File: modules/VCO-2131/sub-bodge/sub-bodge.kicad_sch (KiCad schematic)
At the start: 2 parts, among them U1 CD4013, U2 SN74HCS74

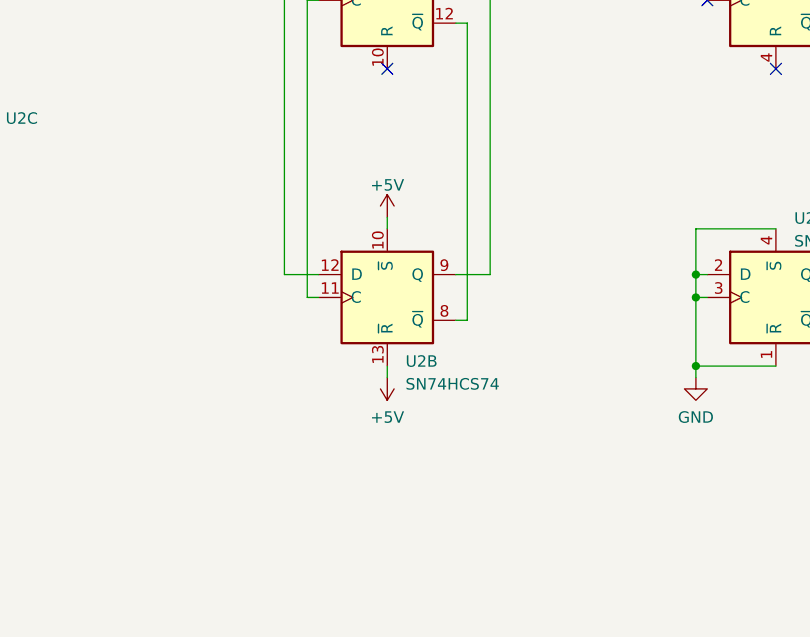
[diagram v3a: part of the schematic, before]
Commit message: VCO sub fix - try again
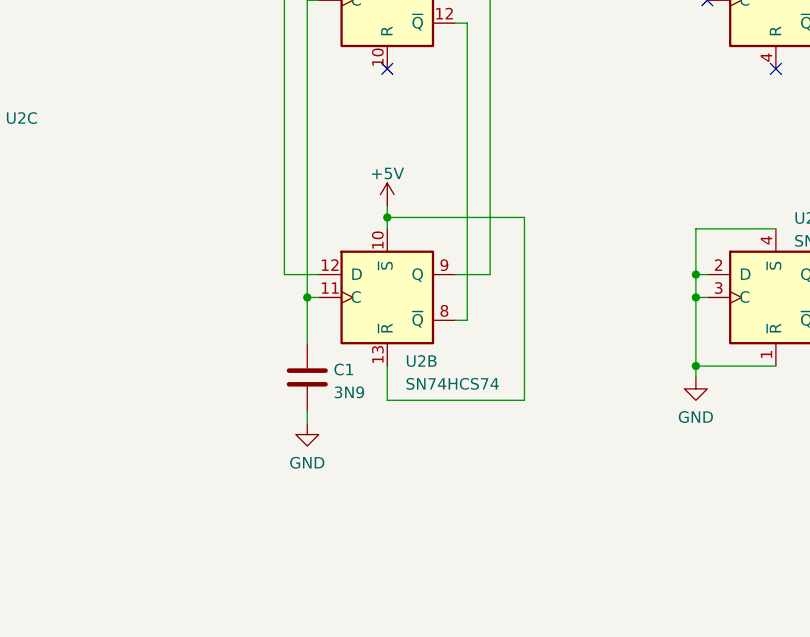
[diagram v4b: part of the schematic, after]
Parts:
- added C1: 3N9, -lmp-misc:C_Rect_Kemet_L7.2mm_W2.5mm_P5mm, symbol -lmp:CF
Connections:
- net GND: now also C1.2
- net at U1.11 (C), U2.11 (C): now also C1.1
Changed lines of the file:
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@@
   (junction (at 177.8 104.14) (diameter 0) (color 0 0 0 0)
+  )
+  (junction (at 143.51 97.79) (diameter 0) (color 0 0 0 0)
+  )
+  (junction (at 134.62 106.68) (diameter 0) (color 0 0 0 0)
   )
   (junction (at 177.8 106.68) (diameter 0) (color 0 0 0 0)
@@
     (stroke (width 0) (type default) (color 0 0 0 0))
   )
+  (wire (pts (xy 143.51 96.52) (xy 143.51 97.79))
+    (stroke (width 0) (type default) (color 0 0 0 0))
+  )
+  (wire (pts (xy 143.51 97.79) (xy 158.75 97.79))
+    (stroke (width 0) (type default) (color 0 0 0 0))
+  )
+  (wire (pts (xy 158.75 97.79) (xy 158.75 118.11))
+    (stroke (width 0) (type default) (color 0 0 0 0))
+  )
+  (wire (pts (xy 134.62 119.38) (xy 134.62 120.65))
+    (stroke (width 0) (type default) (color 0 0 0 0))
+  )
+  (wire (pts (xy 132.08 104.14) (xy 135.89 104.14))
+    (stroke (width 0) (type default) (color 0 0 0 0))
+  )
+  (wire (pts (xy 143.51 114.3) (xy 143.51 118.11))
+    (stroke (width 0) (type default) (color 0 0 0 0))
+  )
+  (wire (pts (xy 78.74 77.47) (xy 78.74 80.01))
+    (stroke (width 0) (type default) (color 0 0 0 0))
+  )
   (wire (pts (xy 143.51 97.79) (xy 143.51 99.06))
     (stroke (width 0) (type default) (color 0 0 0 0))
   )
-  (wire (pts (xy 132.08 104.14) (xy 135.89 104.14))
-    (stroke (width 0) (type default) (color 0 0 0 0))
-  )
-  (wire (pts (xy 143.51 114.3) (xy 143.51 115.57))
-    (stroke (width 0) (type default) (color 0 0 0 0))
-  )
-  (wire (pts (xy 78.74 77.47) (xy 78.74 80.01))
-    (stroke (width 0) (type default) (color 0 0 0 0))
-  )
   (wire (pts (xy 177.8 114.3) (xy 186.69 114.3))
     (stroke (width 0) (type default) (color 0 0 0 0))
@@
     (stroke (width 0) (type default) (color 0 0 0 0))
   )
+  (wire (pts (xy 143.51 118.11) (xy 158.75 118.11))
+    (stroke (width 0) (type default) (color 0 0 0 0))
+  )
   (wire (pts (xy 152.4 76.2) (xy 152.4 109.22))
     (stroke (width 0) (type default) (color 0 0 0 0))
   )
   (wire (pts (xy 177.8 104.14) (xy 179.07 104.14))
+    (stroke (width 0) (type default) (color 0 0 0 0))
+  )
+  (wire (pts (xy 134.62 106.68) (xy 134.62 111.76))
     (stroke (width 0) (type default) (color 0 0 0 0))
   )
@@
   (symbol (lib_id "-lmp-power:+5V") (at 78.74 77.47 0) (unit 1)
     (in_bom yes) (on_board yes) (fields_autoplaced)
-    (property "Reference" "#PWR0108" (id 0) (at 78.74 81.28 0)
+    (property "Reference" "#PWR01" (id 0) (at 78.74 81.28 0)
       (effects (font (size 1.27 1.27)) hide)
     )
@@
     (pin "1")
   )
+  (symbol (lib_id "-lmp:CF") (at 134.62 115.57 0) (unit 1)
+    (in_bom yes) (on_board yes) (fields_autoplaced)
+    (property "Reference" "C1" (id 0) (at 137.541 114.7353 0)
+      (effects (font (size 1.27 1.27)) (justify left))
+    )
+    (property "Value" "3N9" (id 1) (at 137.541 117.2722 0)
+      (effects (font (size 1.27 1.27)) (justify left))
+    )
+    (property "Footprint" "-lmp-misc:C_Rect_Kemet_L7.2mm_W2.5mm_P5mm" (id 2) (at 135.5852 119.38 0)
+      (effects (font (size 1.27 1.27)) hide)
+    )
+    (property "Datasheet" "~" (id 3) (at 134.62 115.57 0)
+      (effects (font (size 1.27 1.27)) hide)
+    )
+    (pin "1")
+    (pin "2")
+  )
   (symbol (lib_id "-lmp-IC-misc:CD4013") (at 186.69 73.66 0) (unit 1)
     (in_bom yes) (on_board yes) (fields_autoplaced)
@@
   (symbol (lib_id "-lmp-power:GND") (at 78.74 97.79 0) (unit 1)
     (in_bom yes) (on_board yes) (fields_autoplaced)
-    (property "Reference" "#PWR0107" (id 0) (at 78.74 104.14 0)
+    (property "Reference" "#PWR02" (id 0) (at 78.74 104.14 0)
       (effects (font (size 1.27 1.27)) hide)
     )
@@
     (pin "7")
   )
-  (symbol (lib_id "-lmp-power:+5V") (at 143.51 97.79 0) (unit 1)
-    (in_bom yes) (on_board yes) (fields_autoplaced)
-    (property "Reference" "#PWR0106" (id 0) (at 143.51 101.6 0)
-      (effects (font (size 1.27 1.27)) hide)
-    )
-    (property "Value" "+5V" (id 1) (at 143.51 94.2142 0))
-    (property "Footprint" "" (id 2) (at 143.51 97.79 0)
-      (effects (font (size 1.27 1.27)) hide)
-    )
-    (property "Datasheet" "" (id 3) (at 143.51 97.79 0)
+  (symbol (lib_id "-lmp-power:+5V") (at 143.51 96.52 0) (unit 1)
+    (in_bom yes) (on_board yes) (fields_autoplaced)
+    (property "Reference" "#PWR04" (id 0) (at 143.51 100.33 0)
+      (effects (font (size 1.27 1.27)) hide)
+    )
+    (property "Value" "+5V" (id 1) (at 143.51 92.9442 0))
+    (property "Footprint" "" (id 2) (at 143.51 96.52 0)
+      (effects (font (size 1.27 1.27)) hide)
+    )
+    (property "Datasheet" "" (id 3) (at 143.51 96.52 0)
       (effects (font (size 1.27 1.27)) hide)
     )
@@
   (symbol (lib_id "-lmp-power:GND") (at 177.8 115.57 0) (unit 1)
     (in_bom yes) (on_board yes) (fields_autoplaced)
-    (property "Reference" "#PWR0102" (id 0) (at 177.8 121.92 0)
+    (property "Reference" "#PWR05" (id 0) (at 177.8 121.92 0)
       (effects (font (size 1.27 1.27)) hide)
     )
@@
     (pin "1")
   )
-  (symbol (lib_id "-lmp-power:+5V") (at 143.51 115.57 180) (unit 1)
-    (in_bom yes) (on_board yes) (fields_autoplaced)
-    (property "Reference" "#PWR0105" (id 0) (at 143.51 111.76 0)
-      (effects (font (size 1.27 1.27)) hide)
-    )
-    (property "Value" "+5V" (id 1) (at 143.51 120.0134 0))
-    (property "Footprint" "" (id 2) (at 143.51 115.57 0)
-      (effects (font (size 1.27 1.27)) hide)
-    )
-    (property "Datasheet" "" (id 3) (at 143.51 115.57 0)
-      (effects (font (size 1.27 1.27)) hide)
-    )
-    (pin "1")
-  )
   (symbol (lib_id "-lmp-IC-misc:SN74HCS74") (at 186.69 106.68 0) (unit 1)
     (in_bom yes) (on_board yes) (fields_autoplaced)
@@
     (pin "14")
     (pin "7")
+  )
+  (symbol (lib_id "-lmp-power:GND") (at 134.62 120.65 0) (unit 1)
+    (in_bom yes) (on_board yes) (fields_autoplaced)
+    (property "Reference" "#PWR03" (id 0) (at 134.62 127 0)
+      (effects (font (size 1.27 1.27)) hide)
+    )
+    (property "Value" "GND" (id 1) (at 134.62 125.0934 0))
+    (property "Footprint" "" (id 2) (at 134.62 120.65 0)
+      (effects (font (size 1.27 1.27)) hide)
+    )
+    (property "Datasheet" "" (id 3) (at 134.62 120.65 0)
+      (effects (font (size 1.27 1.27)) hide)
+    )
+    (pin "1")
   )
   (symbol (lib_id "-lmp-IC-misc:CD4013") (at 74.93 87.63 0) (unit 3)
@@
   )
   (symbol_instances
+    (path "/25dda71c-2a69-4524-8f0a-227178fc174f"
+      (reference "#PWR01") (unit 1) (value "+5V") (footprint "")
+    )
+    (path "/6993a097-434f-4b49-b862-84b8c90b2e2f"
+      (reference "#PWR02") (unit 1) (value "GND") (footprint "")
+    )
+    (path "/eea7292b-3db7-428b-87dc-4f70e2913c01"
+      (reference "#PWR03") (unit 1) (value "GND") (footprint "")
+    )
+    (path "/6fcc877b-cc25-46bd-a4d5-1d2a07146d4a"
+      (reference "#PWR04") (unit 1) (value "+5V") (footprint "")
+    )
     (path "/7aea6cd1-07b8-4471-bbad-48d20bc35787"
-      (reference "#PWR0102") (unit 1) (value "GND") (footprint "")
-    )
-    (path "/7be196fb-6a74-48a7-8f58-6beebbe737b3"
-      (reference "#PWR0105") (unit 1) (value "+5V") (footprint "")
-    )
-    (path "/6fcc877b-cc25-46bd-a4d5-1d2a07146d4a"
-      (reference "#PWR0106") (unit 1) (value "+5V") (footprint "")
-    )
-    (path "/6993a097-434f-4b49-b862-84b8c90b2e2f"
-      (reference "#PWR0107") (unit 1) (value "GND") (footprint "")
-    )
-    (path "/25dda71c-2a69-4524-8f0a-227178fc174f"
-      (reference "#PWR0108") (unit 1) (value "+5V") (footprint "")
+      (reference "#PWR05") (unit 1) (value "GND") (footprint "")
+    )
+    (path "/3f1e70a7-ecc0-4841-946e-e4cadf1fcc8e"
+      (reference "C1") (unit 1) (value "3N9") (footprint "-lmp-misc:C_Rect_Kemet_L7.2mm_W2.5mm_P5mm")
     )
     (path "/564c737a-c22b-400c-8665-990100e2bad2"

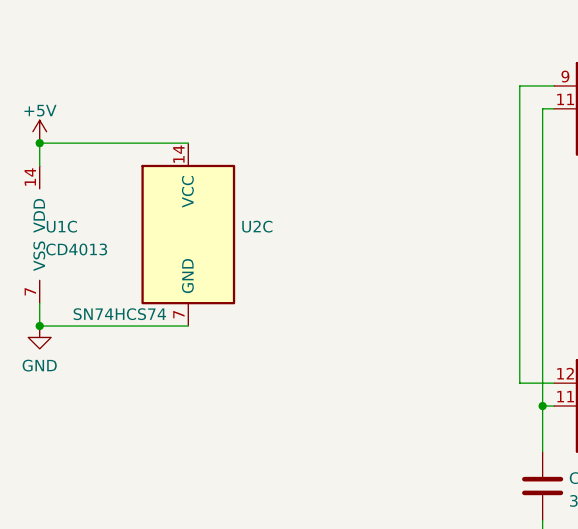
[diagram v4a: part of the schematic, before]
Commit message: VCO sub fix - change library symbol
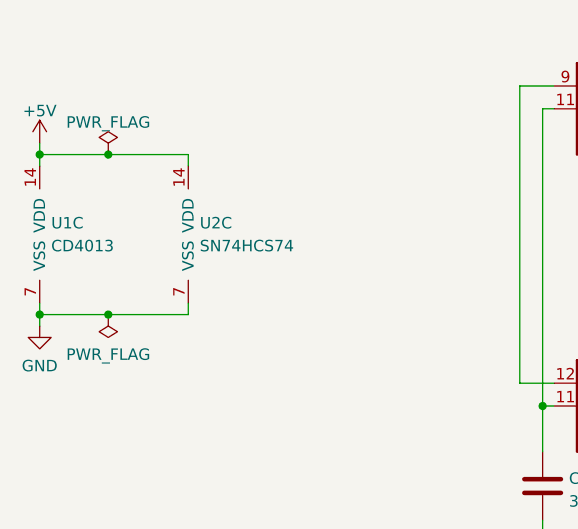
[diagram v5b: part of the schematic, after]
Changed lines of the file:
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@@
     (comment 2 "Bodge board to fix sub-oscillator")
   )
+  (junction (at 86.36 96.52) (diameter 0) (color 0 0 0 0)
+  )
   (junction (at 177.8 104.14) (diameter 0) (color 0 0 0 0)
   )
@@
   (junction (at 177.8 106.68) (diameter 0) (color 0 0 0 0)
   )
-  (junction (at 78.74 97.79) (diameter 0) (color 0 0 0 0)
-  )
-  (junction (at 78.74 77.47) (diameter 0) (color 0 0 0 0)
+  (junction (at 78.74 96.52) (diameter 0) (color 0 0 0 0)
+  )
+  (junction (at 78.74 78.74) (diameter 0) (color 0 0 0 0)
+  )
+  (junction (at 86.36 78.74) (diameter 0) (color 0 0 0 0)
   )
   (junction (at 177.8 114.3) (diameter 0) (color 0 0 0 0)
@@
     (stroke (width 0) (type default) (color 0 0 0 0))
   )
+  (wire (pts (xy 86.36 96.52) (xy 95.25 96.52))
+    (stroke (width 0) (type default) (color 0 0 0 0))
+  )
   (wire (pts (xy 177.8 114.3) (xy 177.8 115.57))
     (stroke (width 0) (type default) (color 0 0 0 0))
@@
     (stroke (width 0) (type default) (color 0 0 0 0))
   )
+  (wire (pts (xy 95.25 78.74) (xy 95.25 80.01))
+    (stroke (width 0) (type default) (color 0 0 0 0))
+  )
   (wire (pts (xy 143.51 114.3) (xy 143.51 118.11))
     (stroke (width 0) (type default) (color 0 0 0 0))
   )
-  (wire (pts (xy 78.74 77.47) (xy 78.74 80.01))
+  (wire (pts (xy 78.74 77.47) (xy 78.74 78.74))
     (stroke (width 0) (type default) (color 0 0 0 0))
   )
@@
     (stroke (width 0) (type default) (color 0 0 0 0))
   )
+  (wire (pts (xy 78.74 96.52) (xy 78.74 97.79))
+    (stroke (width 0) (type default) (color 0 0 0 0))
+  )
   (wire (pts (xy 134.62 106.68) (xy 134.62 111.76))
     (stroke (width 0) (type default) (color 0 0 0 0))
   )
+  (wire (pts (xy 95.25 95.25) (xy 95.25 96.52))
+    (stroke (width 0) (type default) (color 0 0 0 0))
+  )
   (wire (pts (xy 154.94 71.12) (xy 154.94 104.14))
     (stroke (width 0) (type default) (color 0 0 0 0))
   )
-  (wire (pts (xy 78.74 97.79) (xy 95.25 97.79))
+  (wire (pts (xy 78.74 96.52) (xy 86.36 96.52))
     (stroke (width 0) (type default) (color 0 0 0 0))
   )
@@
     (stroke (width 0) (type default) (color 0 0 0 0))
   )
+  (wire (pts (xy 78.74 78.74) (xy 78.74 80.01))
+    (stroke (width 0) (type default) (color 0 0 0 0))
+  )
+  (wire (pts (xy 86.36 78.74) (xy 95.25 78.74))
+    (stroke (width 0) (type default) (color 0 0 0 0))
+  )
   (wire (pts (xy 151.13 71.12) (xy 154.94 71.12))
     (stroke (width 0) (type default) (color 0 0 0 0))
   )
-  (wire (pts (xy 78.74 95.25) (xy 78.74 97.79))
+  (wire (pts (xy 78.74 95.25) (xy 78.74 96.52))
     (stroke (width 0) (type default) (color 0 0 0 0))
   )
@@
     (stroke (width 0) (type default) (color 0 0 0 0))
   )
-  (wire (pts (xy 78.74 77.47) (xy 95.25 77.47))
+  (wire (pts (xy 78.74 78.74) (xy 86.36 78.74))
     (stroke (width 0) (type default) (color 0 0 0 0))
   )
@@
     (pin "2")
   )
+  (symbol (lib_id "-lmp-power:PWR_FLAG") (at 86.36 78.74 0) (unit 1)
+    (in_bom yes) (on_board yes) (fields_autoplaced)
+    (property "Reference" "#FLG01" (id 0) (at 86.36 76.835 0)
+      (effects (font (size 1.27 1.27)) hide)
+    )
+    (property "Value" "PWR_FLAG" (id 1) (at 86.36 75.1642 0))
+    (property "Footprint" "" (id 2) (at 86.36 78.74 0)
+      (effects (font (size 1.27 1.27)) hide)
+    )
+    (property "Datasheet" "~" (id 3) (at 86.36 78.74 0)
+      (effects (font (size 1.27 1.27)) hide)
+    )
+    (pin "1")
+  )
   (symbol (lib_id "-lmp-IC-misc:CD4013") (at 186.69 73.66 0) (unit 1)
     (in_bom yes) (on_board yes) (fields_autoplaced)
@@
     (pin "7")
   )
-  (symbol (lib_id "-lmp-IC-misc:SN74HCS74") (at 95.25 87.63 0) (unit 3)
-    (in_bom yes) (on_board yes) (fields_autoplaced)
-    (property "Reference" "U2" (id 0) (at 101.092 86.7953 0)
-      (effects (font (size 1.27 1.27)) (justify left))
-    )
-    (property "Value" "SN74HCS74" (id 1) (at 87.63 96.52 0))
+  (symbol (lib_name "SN74HCS74_1") (lib_id "-lmp-IC-misc:SN74HCS74") (at 95.25 87.63 0) (unit 3)
+    (in_bom yes) (on_board yes)
+    (property "Reference" "U2" (id 0) (at 96.52 86.36 0)
+      (effects (font (size 1.27 1.27)) (justify left))
+    )
+    (property "Value" "SN74HCS74" (id 1) (at 96.52 88.9 0)
+      (effects (font (size 1.27 1.27)) (justify left))
+    )
     (property "Footprint" "Package_SO:SOIC-14_3.9x8.7mm_P1.27mm" (id 2) (at 95.25 87.63 0)
       (effects (font (size 1.27 1.27)) hide)
@@
     (pin "1")
   )
-  (symbol (lib_id "-lmp-IC-misc:SN74HCS74") (at 186.69 106.68 0) (unit 1)
+  (symbol (lib_name "SN74HCS74_2") (lib_id "-lmp-IC-misc:SN74HCS74") (at 186.69 106.68 0) (unit 1)
     (in_bom yes) (on_board yes) (fields_autoplaced)
     (property "Reference" "U2" (id 0) (at 188.7094 97.9002 0)
@@
     (pin "1")
   )
+  (symbol (lib_id "-lmp-power:PWR_FLAG") (at 86.36 96.52 180) (unit 1)
+    (in_bom yes) (on_board yes) (fields_autoplaced)
+    (property "Reference" "#FLG02" (id 0) (at 86.36 98.425 0)
+      (effects (font (size 1.27 1.27)) hide)
+    )
+    (property "Value" "PWR_FLAG" (id 1) (at 86.36 100.9634 0))
+    (property "Footprint" "" (id 2) (at 86.36 96.52 0)
+      (effects (font (size 1.27 1.27)) hide)
+    )
+    (property "Datasheet" "~" (id 3) (at 86.36 96.52 0)
+      (effects (font (size 1.27 1.27)) hide)
+    )
+    (pin "1")
+  )
   (symbol (lib_id "-lmp-IC-misc:CD4013") (at 74.93 87.63 0) (unit 3)
-    (in_bom yes) (on_board yes) (fields_autoplaced)
-    (property "Reference" "U1" (id 0) (at 79.375 86.7953 0)
-      (effects (font (size 1.27 1.27)) (justify left))
-    )
-    (property "Value" "CD4013" (id 1) (at 79.375 89.3322 0)
+    (in_bom yes) (on_board yes)
+    (property "Reference" "U1" (id 0) (at 80.01 86.36 0)
+      (effects (font (size 1.27 1.27)) (justify left))
+    )
+    (property "Value" "CD4013" (id 1) (at 80.01 88.9 0)
       (effects (font (size 1.27 1.27)) (justify left))
     )
@@
   )
   (symbol_instances
+    (path "/55e34010-467f-4d03-a3cf-6eee79fb56e6"
+      (reference "#FLG01") (unit 1) (value "PWR_FLAG") (footprint "")
+    )
+    (path "/eeeba0dc-393b-4399-989f-34c9317c3d91"
+      (reference "#FLG02") (unit 1) (value "PWR_FLAG") (footprint "")
+    )
     (path "/25dda71c-2a69-4524-8f0a-227178fc174f"
       (reference "#PWR01") (unit 1) (value "+5V") (footprint "")

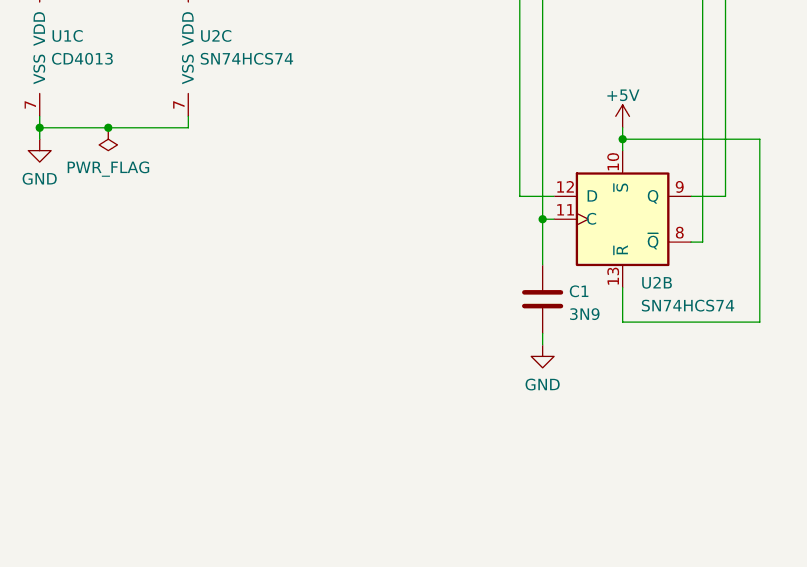
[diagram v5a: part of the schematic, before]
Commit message: VCO sub fix - TODOs
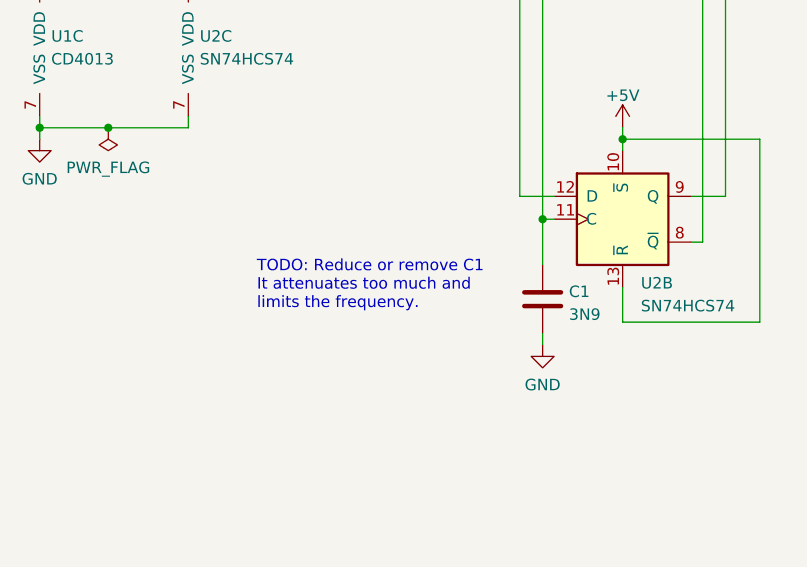
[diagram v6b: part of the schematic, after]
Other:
- note added: "TODO: Reduce or remove C1 It attenuates too much and limits the frequency."
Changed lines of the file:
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@@
     (stroke (width 0) (type default) (color 0 0 0 0))
+  )
+  (text "TODO: Reduce or remove C1\nIt attenuates too much and \nlimits the frequency."
+    (at 102.87 116.84 0)
+    (effects (font (size 1.27 1.27)) (justify left bottom))
   )
   (text "All fixed resistors are 1% tolerance unless otherwise specified."

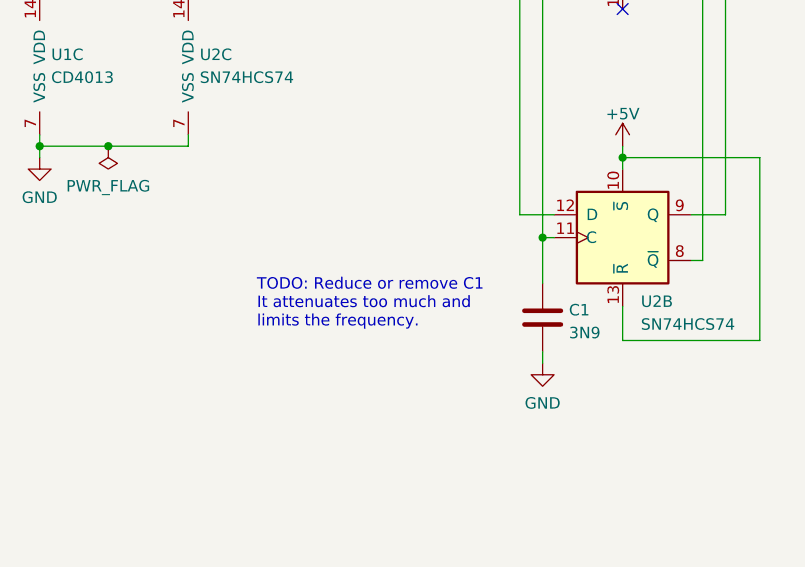
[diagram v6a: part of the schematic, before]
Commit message: VCO sub fix - main module design updated
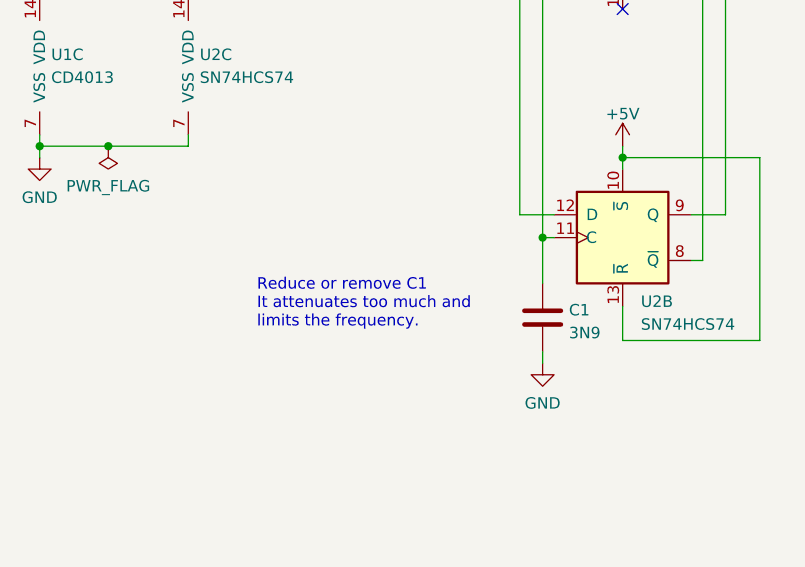
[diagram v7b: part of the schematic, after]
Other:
- note added: "Reduce or remove C1 It attenuates too much and limits the frequency."
- note removed: "TODO: Reduce or remove C1 It attenuates too much and limits the frequency."
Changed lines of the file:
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@@
     (stroke (width 0) (type default) (color 0 0 0 0))
   )
-  (text "TODO: Reduce or remove C1\nIt attenuates too much and \nlimits the frequency."
+  (text "Reduce or remove C1\nIt attenuates too much and \nlimits the frequency."
     (at 102.87 116.84 0)
     (effects (font (size 1.27 1.27)) (justify left bottom))
